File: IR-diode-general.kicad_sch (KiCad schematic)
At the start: 27 parts, among them J1 PJ-102A, J2 USB4105-GF-A, J3 SM06B-SRSS-TB-LF-SN, J4 SM06B-SRSS-TB-LF-SN, U1 MP2483DQ-LF-P, U2 AZ1117CH-5.0TRG1

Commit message: Changed R2
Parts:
- removed R2: R_100k_0402, antmicro-footprints:R_0402_1005Metric, symbol antmicroResistors0402:R_100k_0402
- added R2: R_39k_0402, antmicro-footprints:0402-res, symbol antmicroResistors0402:R_39k_0402
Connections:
- net GND: now also R2.1
- net at C5.2, U1.6 (RSET): now also R2.2
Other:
- note added: "Frequency set to 1MHz"
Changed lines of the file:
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@@
+    (effects (font (size 1.27 1.27)) (justify left bottom))
+  )
+  (text "Frequency set to 1MHz" (at 167.64 177.8 0)
     (effects (font (size 1.27 1.27)) (justify left bottom))
   )
@@
     (pin "1")
   )
-  (symbol (lib_id "antmicroResistors0402:R_100k_0402") (at 175.895 173.355 90) (unit 1)
-    (in_bom yes) (on_board yes) (fields_autoplaced)
-    (property "Reference" "R2" (id 0) (at 178.435 169.5449 90)
+  (symbol (lib_id "antmicroResistors0402:R_39k_0402") (at 175.895 173.355 90) (unit 1)
+    (in_bom yes) (on_board yes) (fields_autoplaced)
+    (property "Reference" "R2" (id 0) (at 177.8 169.5449 90)
       (effects (font (size 1.27 1.27) (thickness 0.15)) (justify right))
     )
-    (property "Value" "R_100k_0402" (id 1) (at 188.595 153.035 0)
-      (effects (font (size 1.27 1.27) (thickness 0.15)) (justify left bottom) hide)
-    )
-    (property "Footprint" "antmicro-footprints:R_0402_1005Metric" (id 2) (at 191.135 153.035 0)
+    (property "Value" "R_39k_0402" (id 1) (at 188.595 153.035 0)
+      (effects (font (size 1.27 1.27) (thickness 0.15)) (justify left bottom) hide)
+    )
+    (property "Footprint" "antmicro-footprints:0402-res" (id 2) (at 191.135 153.035 0)
       (effects (font (size 1.27 1.27) (thickness 0.15)) (justify left bottom) hide)
     )
@@
       (effects (font (size 1.27 1.27) (thickness 0.15)) (justify left bottom) hide)
     )
-    (property "MPN" "CR0402-FX-1003GLF" (id 4) (at 196.215 153.035 0)
+    (property "MPN" "CR0402-FX-3902GLF" (id 4) (at 196.215 153.035 0)
       (effects (font (size 1.27 1.27) (thickness 0.15)) (justify left bottom) hide)
     )
@@
       (effects (font (size 1.27 1.27) (thickness 0.15)) (justify left bottom) hide)
     )
-    (property "Val" "100k" (id 8) (at 178.435 172.0849 90)
+    (property "Val" "39k" (id 8) (at 177.8 172.0849 90)
       (effects (font (size 1.27 1.27) (thickness 0.15)) (justify right))
     )
@@
       (reference "R1") (unit 1) (value "R_0R2_1206") (footprint "antmicro-footprints:1206-res")
     )
-    (path "/a26c0bc8-b005-443c-aab0-266a48967c9e"
-      (reference "R2") (unit 1) (value "R_100k_0402") (footprint "antmicro-footprints:R_0402_1005Metric")
+    (path "/99114cbd-59c4-4ec2-8aec-80348f911fe1"
+      (reference "R2") (unit 1) (value "R_39k_0402") (footprint "antmicro-footprints:0402-res")
     )
     (path "/6c74cd7e-4b19-4587-9be3-8ad57aff1921"

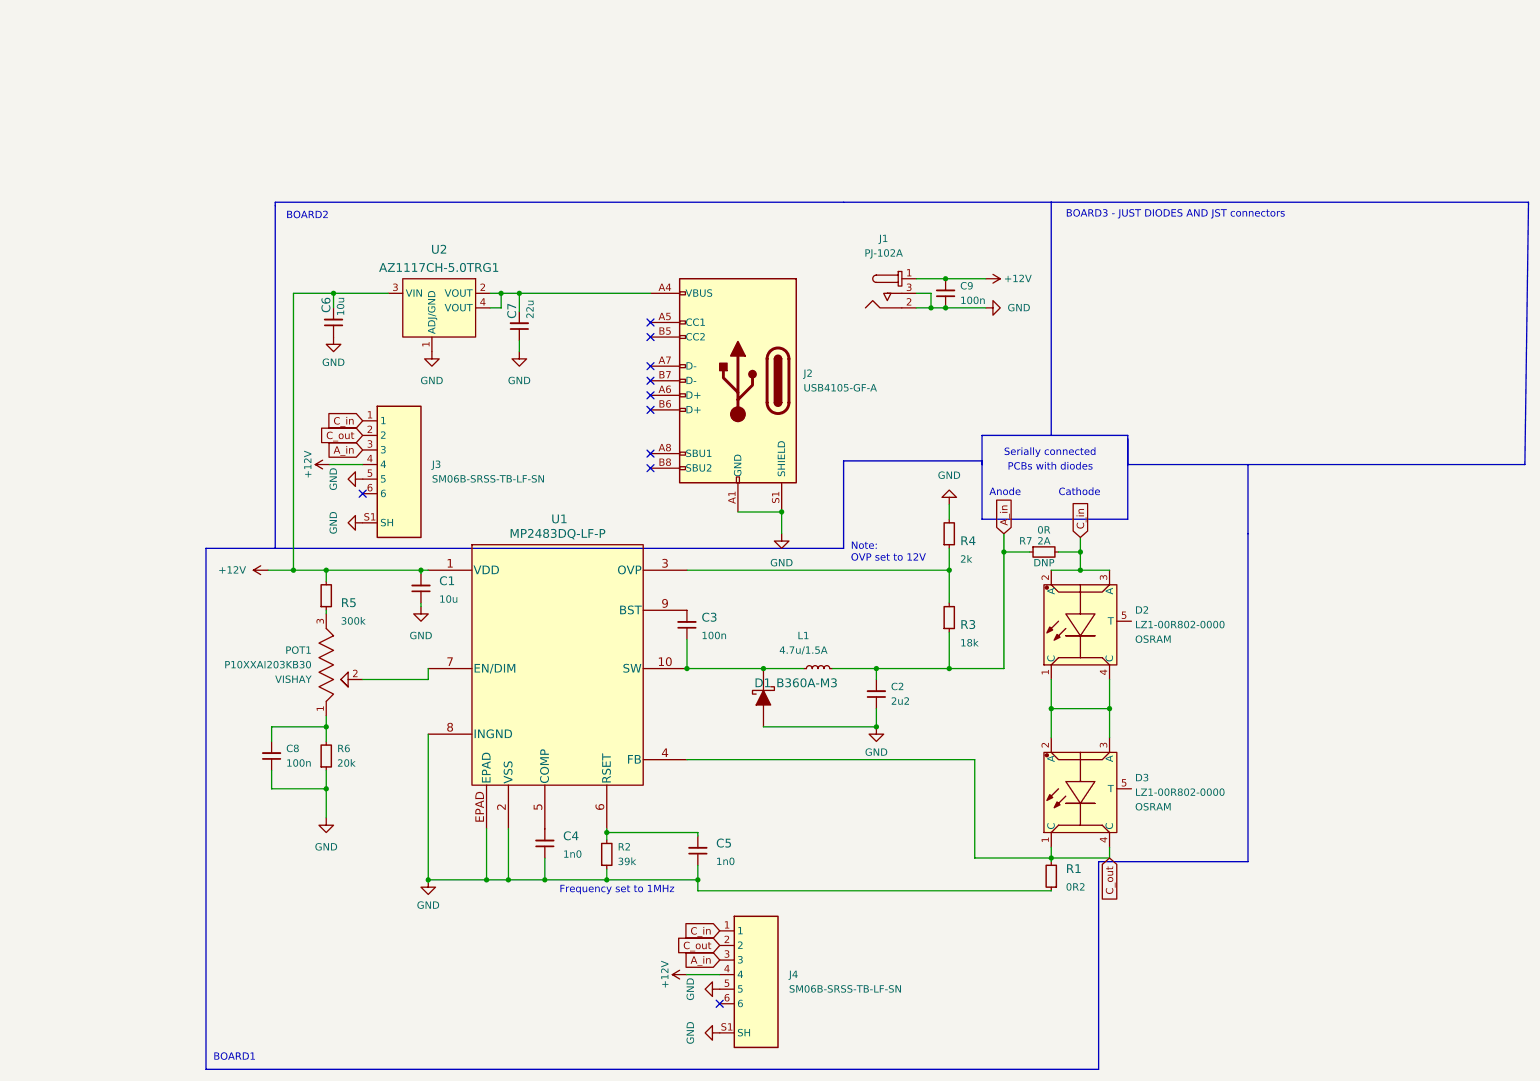
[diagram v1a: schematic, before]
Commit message: Added notes on U1 configuration
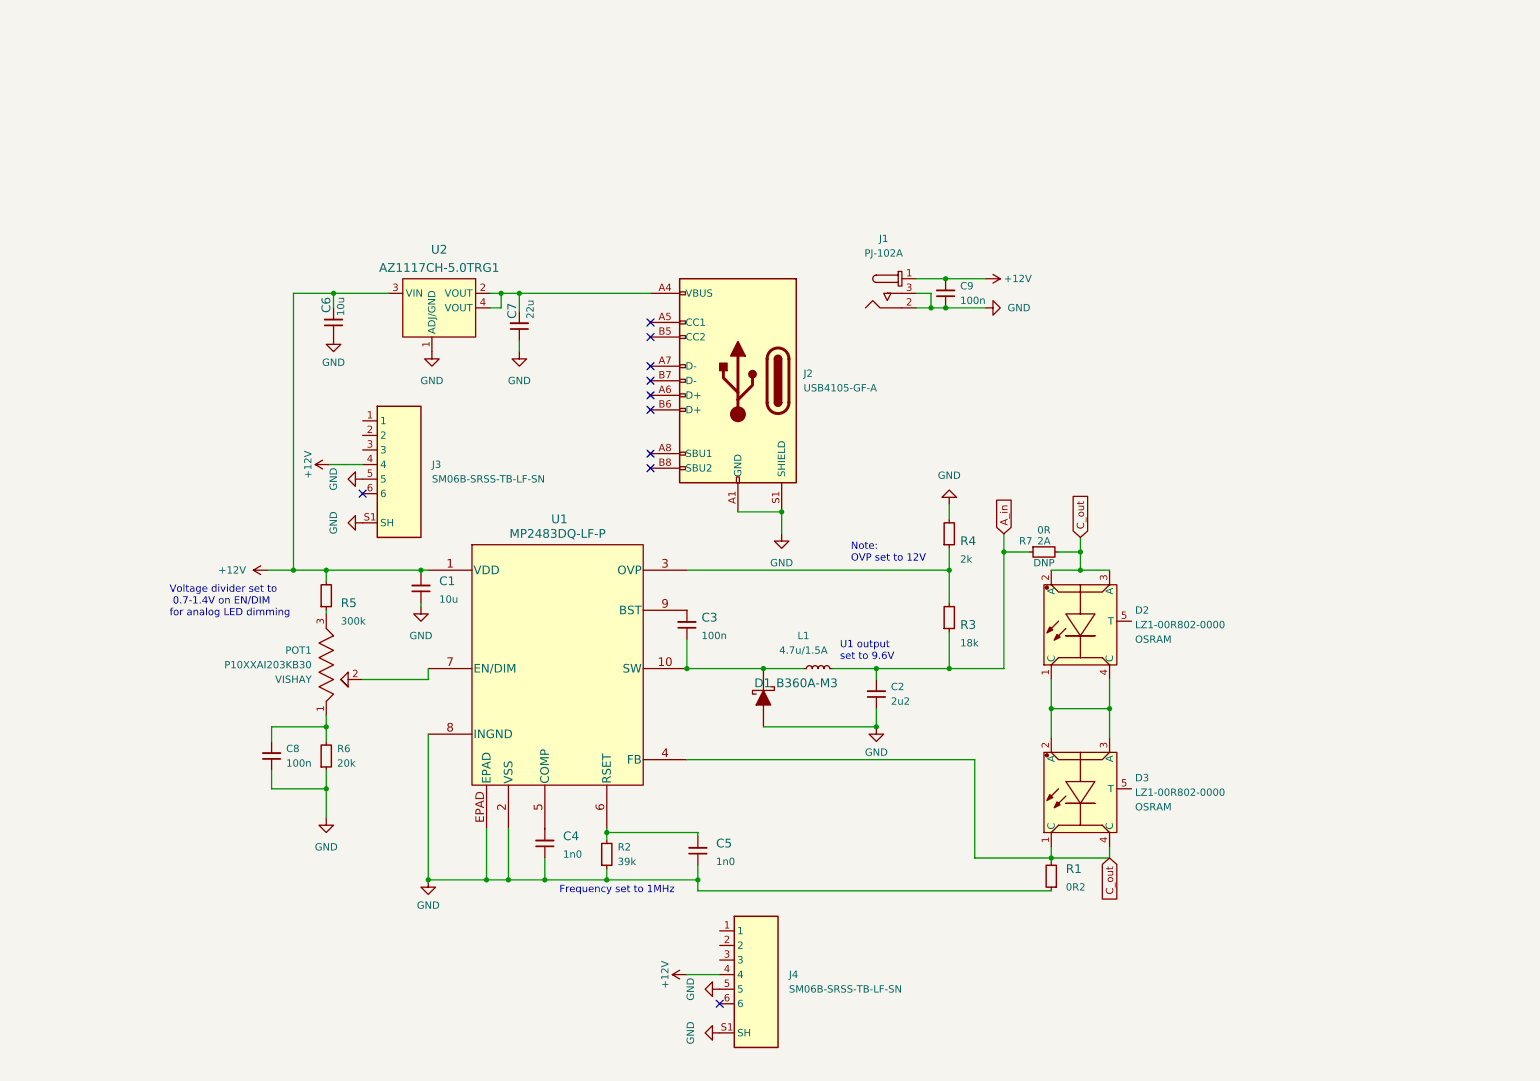
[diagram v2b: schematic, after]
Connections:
- net A_in: no longer J3.3, J4.3
- net C_out: now also D2.2 (A), D2.3 (A), R7.2; no longer J3.2, J4.2
- removed net C_in: D2.2 (A), D2.3 (A), J3.1, J4.1, R7.2
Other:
- note added: "U1 output set to 9.6V"
- note added: "Voltage divider set to 0.7-1.4V on EN/DIM for analog LED dimming"
- note removed: "Anode"
- note removed: "BOARD1"
- note removed: "BOARD2"
- note removed: "BOARD3 - JUST DIODES AND JST connectors"
- note removed: "Cathode"
- note removed: "PCBs with diodes"
- note removed: "Serially connected"
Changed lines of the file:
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@@
   (no_connect (at 183.515 80.645))
   (no_connect (at 183.515 88.265))
-  (polyline (pts (xy 266.7 102.87) (xy 335.915 102.87))
-    (stroke (width 0) (type default) (color 0 0 0 0))
-  )
   (wire (pts (xy 241.935 70.485) (xy 234.95 70.485))
     (stroke (width 0) (type default) (color 0 0 0 0))
   )
-  (polyline (pts (xy 217.17 57.15) (xy 118.11 57.15))
-    (stroke (width 0) (type default) (color 0 0 0 0))
-  )
   (wire (pts (xy 232.41 75.565) (xy 234.95 75.565))
     (stroke (width 0) (type default) (color 0 0 0 0))
@@
     (stroke (width 0) (type default) (color 0 0 0 0))
   )
-  (polyline (pts (xy 106.045 117.475) (xy 106.045 208.28))
-    (stroke (width 0) (type default) (color 0 0 0 0))
-  )
   (wire (pts (xy 144.78 175.26) (xy 154.94 175.26))
     (stroke (width 0) (type default) (color 0 0 0 0))
@@
     (stroke (width 0) (type default) (color 0 0 0 0))
   )
-  (polyline (pts (xy 118.11 57.15) (xy 118.11 57.785))
-    (stroke (width 0) (type default) (color 0 0 0 0))
-  )
   (wire (pts (xy 191.77 167.64) (xy 191.77 167.005))
     (stroke (width 0) (type default) (color 0 0 0 0))
@@
     (stroke (width 0) (type default) (color 0 0 0 0))
   )
-  (polyline (pts (xy 266.7 102.87) (xy 266.7 98.425))
-    (stroke (width 0) (type default) (color 0 0 0 0))
-  )
   (wire (pts (xy 157.48 75.565) (xy 157.48 73.025))
     (stroke (width 0) (type default) (color 0 0 0 0))
@@
     (stroke (width 0) (type default) (color 0 0 0 0))
   )
-  (polyline (pts (xy 287.655 102.87) (xy 287.655 114.935))
-    (stroke (width 0) (type default) (color 0 0 0 0))
-  )
   (wire (pts (xy 235.585 132.08) (xy 235.585 138.43))
     (stroke (width 0) (type default) (color 0 0 0 0))
@@
     (stroke (width 0) (type default) (color 0 0 0 0))
   )
-  (polyline (pts (xy 287.655 172.085) (xy 287.655 114.935))
-    (stroke (width 0) (type default) (color 0 0 0 0))
-  )
   (wire (pts (xy 253.365 172.085) (xy 253.365 171.45))
     (stroke (width 0) (type default) (color 0 0 0 0))
@@
     (stroke (width 0) (type default) (color 0 0 0 0))
   )
-  (polyline (pts (xy 241.3 112.395) (xy 266.7 112.395))
-    (stroke (width 0) (type default) (color 0 0 0 0))
-  )
-  (polyline (pts (xy 266.7 97.79) (xy 241.3 97.79))
-    (stroke (width 0) (type default) (color 0 0 0 0))
-  )
   (wire (pts (xy 229.87 70.485) (xy 234.95 70.485))
     (stroke (width 0) (type default) (color 0 0 0 0))
@@
     (stroke (width 0) (type default) (color 0 0 0 0))
   )
-  (polyline (pts (xy 261.62 208.28) (xy 261.62 172.085))
-    (stroke (width 0) (type default) (color 0 0 0 0))
-  )
   (wire (pts (xy 117.475 156.21) (xy 117.475 159.385))
     (stroke (width 0) (type default) (color 0 0 0 0))
@@
     (stroke (width 0) (type default) (color 0 0 0 0))
   )
-  (polyline (pts (xy 118.11 117.475) (xy 217.17 117.475))
-    (stroke (width 0) (type default) (color 0 0 0 0))
-  )
   (wire (pts (xy 222.885 138.43) (xy 235.585 138.43))
     (stroke (width 0) (type default) (color 0 0 0 0))
@@
     (stroke (width 0) (type default) (color 0 0 0 0))
   )
-  (polyline (pts (xy 118.11 117.475) (xy 106.045 117.475))
-    (stroke (width 0) (type default) (color 0 0 0 0))
-  )
-  (polyline (pts (xy 241.3 102.235) (xy 241.3 102.87))
-    (stroke (width 0) (type default) (color 0 0 0 0))
-  )
-  (polyline (pts (xy 253.365 57.15) (xy 253.365 97.79))
-    (stroke (width 0) (type default) (color 0 0 0 0))
-  )
-  (polyline (pts (xy 261.62 172.085) (xy 287.655 172.085))
-    (stroke (width 0) (type default) (color 0 0 0 0))
-  )
   (wire (pts (xy 191.77 177.165) (xy 191.77 175.26))
     (stroke (width 0) (type default) (color 0 0 0 0))
@@
     (stroke (width 0) (type default) (color 0 0 0 0))
   )
-  (polyline (pts (xy 266.7 112.395) (xy 266.7 97.79))
-    (stroke (width 0) (type default) (color 0 0 0 0))
-  )
   (wire (pts (xy 117.475 159.385) (xy 127 159.385))
     (stroke (width 0) (type default) (color 0 0 0 0))
@@
     (stroke (width 0) (type default) (color 0 0 0 0))
   )
-  (polyline (pts (xy 217.17 117.475) (xy 217.17 102.235))
-    (stroke (width 0) (type default) (color 0 0 0 0))
-  )
   (wire (pts (xy 117.475 151.13) (xy 117.475 148.59))
     (stroke (width 0) (type default) (color 0 0 0 0))
@@
     (stroke (width 0) (type default) (color 0 0 0 0))
   )
-  (polyline (pts (xy 253.365 57.15) (xy 336.55 57.15))
-    (stroke (width 0) (type default) (color 0 0 0 0))
-  )
   (wire (pts (xy 128.27 73.025) (xy 137.795 73.025))
     (stroke (width 0) (type default) (color 0 0 0 0))
@@
     (stroke (width 0) (type default) (color 0 0 0 0))
   )
-  (polyline (pts (xy 336.55 57.15) (xy 335.915 102.87))
-    (stroke (width 0) (type default) (color 0 0 0 0))
-  )
-  (polyline (pts (xy 241.3 97.79) (xy 241.3 112.395))
-    (stroke (width 0) (type default) (color 0 0 0 0))
-  )
-  (polyline (pts (xy 118.11 57.785) (xy 118.11 117.475))
-    (stroke (width 0) (type default) (color 0 0 0 0))
-  )
   (wire (pts (xy 154.94 175.26) (xy 158.75 175.26))
     (stroke (width 0) (type default) (color 0 0 0 0))
@@
     (stroke (width 0) (type default) (color 0 0 0 0))
   )
-  (polyline (pts (xy 106.045 208.28) (xy 261.62 208.28))
-    (stroke (width 0) (type default) (color 0 0 0 0))
-  )
   (wire (pts (xy 253.365 140.335) (xy 253.365 145.415))
     (stroke (width 0) (type default) (color 0 0 0 0))
   )
-  (polyline (pts (xy 217.17 57.15) (xy 253.365 57.15))
-    (stroke (width 0) (type default) (color 0 0 0 0))
-  )
   (wire (pts (xy 189.865 133.35) (xy 189.865 138.43))
     (stroke (width 0) (type default) (color 0 0 0 0))
@@
     (stroke (width 0) (type default) (color 0 0 0 0))
   )
-  (polyline (pts (xy 217.17 102.235) (xy 241.3 102.235))
-    (stroke (width 0) (type default) (color 0 0 0 0))
-  )
   (wire (pts (xy 263.525 145.415) (xy 263.525 150.495))
     (stroke (width 0) (type default) (color 0 0 0 0))
-  )
-  (text "Anode\n" (at 242.57 108.585 0)
-    (effects (font (size 1.27 1.27)) (justify left bottom))
-  )
-  (text "Serially connected " (at 245.11 101.6 0)
-    (effects (font (size 1.27 1.27)) (justify left bottom))
   )
   (text "Note: \nOVP set to 12V" (at 218.44 120.015 0)
     (effects (font (size 1.27 1.27)) (justify left bottom))
   )
-  (text "Cathode\n" (at 254.635 108.585 0)
-    (effects (font (size 1.27 1.27)) (justify left bottom))
-  )
-  (text "BOARD3 - JUST DIODES AND JST connectors\n\n\n" (at 255.905 64.135 0)
-    (effects (font (size 1.27 1.27)) (justify left bottom))
-  )
-  (text "PCBs with diodes" (at 245.745 104.14 0)
+  (text "Voltage divider set to\n 0.7-1.4V on EN/DIM\nfor analog LED dimming"
+    (at 99.695 129.54 0)
     (effects (font (size 1.27 1.27)) (justify left bottom))
   )
@@
     (effects (font (size 1.27 1.27)) (justify left bottom))
   )
-  (text "BOARD1\n" (at 107.315 207.01 0)
+  (text "U1 output\nset to 9.6V\n" (at 216.535 137.16 0)
     (effects (font (size 1.27 1.27)) (justify left bottom))
-  )
-  (text "BOARD2\n" (at 120.015 60.325 0)
-    (effects (font (size 1.27 1.27)) (justify left bottom))
-  )
-  (global_label "C_out" (shape input) (at 195.58 186.69 180) (fields_autoplaced)
-    (effects (font (size 1.27 1.27)) (justify right))
-    (property "Intersheet References" "${INTERSHEET_REFS}" (id 0) (at 187.9055 186.6106 0)
-      (effects (font (size 1.27 1.27)) (justify right) hide)
-    )
   )
   (global_label "A_in" (shape input) (at 245.11 114.935 90) (fields_autoplaced)
@@
     )
   )
-  (global_label "C_out" (shape input) (at 133.35 97.79 180) (fields_autoplaced)
-    (effects (font (size 1.27 1.27)) (justify right))
-    (property "Intersheet References" "${INTERSHEET_REFS}" (id 0) (at 125.6755 97.7106 0)
-      (effects (font (size 1.27 1.27)) (justify right) hide)
-    )
-  )
-  (global_label "C_in" (shape input) (at 133.35 95.25 180) (fields_autoplaced)
-    (effects (font (size 1.27 1.27)) (justify right))
-    (property "Intersheet References" "${INTERSHEET_REFS}" (id 0) (at 126.9455 95.1706 0)
-      (effects (font (size 1.27 1.27)) (justify right) hide)
-    )
-  )
-  (global_label "A_in" (shape input) (at 195.58 189.23 180) (fields_autoplaced)
-    (effects (font (size 1.27 1.27)) (justify right))
-    (property "Intersheet References" "${INTERSHEET_REFS}" (id 0) (at 189.3569 189.1506 0)
-      (effects (font (size 1.27 1.27)) (justify right) hide)
-    )
-  )
-  (global_label "C_in" (shape input) (at 258.445 115.57 90) (fields_autoplaced)
+  (global_label "C_out" (shape input) (at 258.445 115.57 90) (fields_autoplaced)
     (effects (font (size 1.27 1.27)) (justify left))
-    (property "Intersheet References" "${INTERSHEET_REFS}" (id 0) (at 258.3656 109.1655 90)
+    (property "Intersheet References" "${INTERSHEET_REFS}" (id 0) (at 258.3656 107.8955 90)
       (effects (font (size 1.27 1.27)) (justify left) hide)
     )
@@
       (effects (font (size 1.27 1.27)) (justify right) hide)
     )
-  )
-  (global_label "C_in" (shape input) (at 195.58 184.15 180) (fields_autoplaced)
-    (effects (font (size 1.27 1.27)) (justify right))
-    (property "Intersheet References" "${INTERSHEET_REFS}" (id 0) (at 189.1755 184.0706 0)
-      (effects (font (size 1.27 1.27)) (justify right) hide)
-    )
-  )
-  (global_label "A_in" (shape input) (at 133.35 100.33 180) (fields_autoplaced)
-    (effects (font (size 1.27 1.27)) (justify right))
-    (property "Intersheet References" "${INTERSHEET_REFS}" (id 0) (at 127.1269 100.2506 0)
-      (effects (font (size 1.27 1.27)) (justify right) hide)
-    )
